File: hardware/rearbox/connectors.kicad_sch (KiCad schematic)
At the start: 6 parts, among them J3 Autosport, J4 Auxiliary

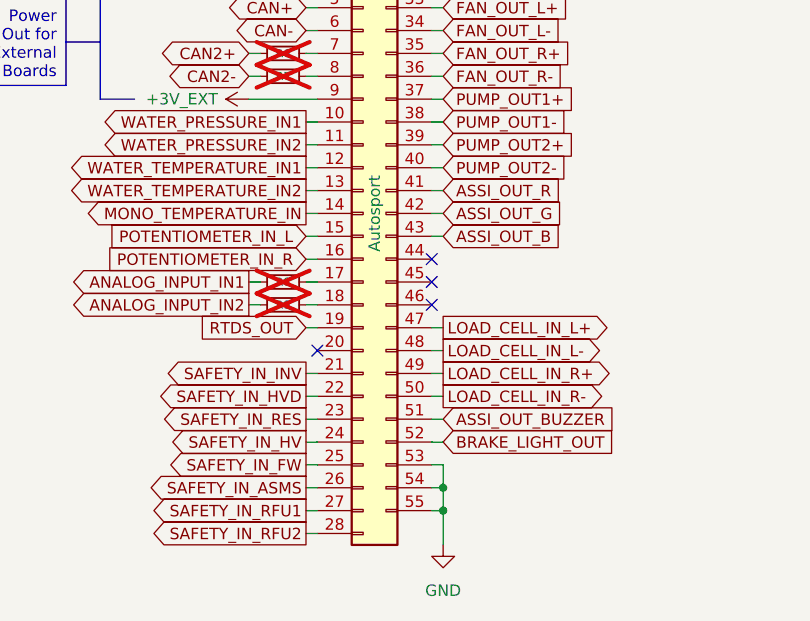
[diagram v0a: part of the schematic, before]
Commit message: Add the connector board
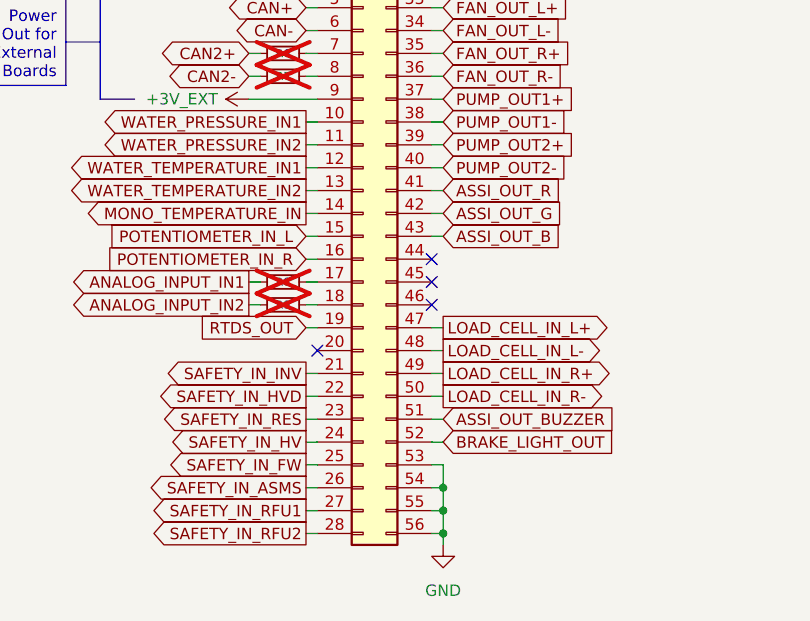
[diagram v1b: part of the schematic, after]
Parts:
- removed J3: Autosport, Local_Library:AS022-55SN, symbol AS022-55SN:AS022-55SN
- added J3: Conn_02x28_Top_Bottom, Connector_PinSocket_2.54mm:PinSocket_2x28_P2.54mm_Horizontal, symbol Connector_Generic:Conn_02x28_Top_Bottom
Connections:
- net +24V: now also J3.1 (Pin_1), J3.2 (Pin_2), J3.3 (Pin_3)
- net +3V_EXT: now also J3.9 (Pin_9)
- net +5V_EXT: now also J3.4 (Pin_4)
- net ASSI_OUT_B: now also J3.43 (Pin_43)
- net ASSI_OUT_BUZZER: now also J3.51 (Pin_51)
- net ASSI_OUT_G: now also J3.42 (Pin_42)
- net ASSI_OUT_R: now also J3.41 (Pin_41)
- net BRAKE_LIGHT_OUT: now also J3.52 (Pin_52)
- net CAN+: now also J3.5 (Pin_5)
- net CAN-: now also J3.6 (Pin_6)
- net FAN_OUT_L+: now also J3.33 (Pin_33)
- net FAN_OUT_L-: now also J3.34 (Pin_34)
- net FAN_OUT_R+: now also J3.35 (Pin_35)
- net FAN_OUT_R-: now also J3.36 (Pin_36)
- net GND: now also J3.53 (Pin_53), J3.54 (Pin_54), J3.55 (Pin_55), J3.56 (Pin_56)
- net LOAD_CELL_IN_L+: now also J3.47 (Pin_47)
- net LOAD_CELL_IN_L-: now also J3.48 (Pin_48)
- net LOAD_CELL_IN_R+: now also J3.49 (Pin_49)
- net LOAD_CELL_IN_R-: now also J3.50 (Pin_50)
- net MONO_TEMPERATURE_IN: now also J3.14 (Pin_14)
- net POTENTIOMETER_IN_L: now also J3.15 (Pin_15)
- net POTENTIOMETER_IN_R: now also J3.16 (Pin_16)
- net PUMP_OUT1+: now also J3.37 (Pin_37)
- net PUMP_OUT1-: now also J3.38 (Pin_38)
- net PUMP_OUT2+: now also J3.39 (Pin_39)
- net PUMP_OUT2-: now also J3.40 (Pin_40)
- net RTDS_OUT: now also J3.19 (Pin_19)
- net SAFETY_IN_ASMS: now also J3.26 (Pin_26)
- net SAFETY_IN_FW: now also J3.25 (Pin_25)
- net SAFETY_IN_HV: now also J3.24 (Pin_24)
- net SAFETY_IN_HVD: now also J3.22 (Pin_22)
- net SAFETY_IN_INV: now also J3.21 (Pin_21)
- net SAFETY_IN_RES: now also J3.23 (Pin_23)
- net SAFETY_IN_RFU1: now also J3.27 (Pin_27)
- net SAFETY_IN_RFU2: now also J3.28 (Pin_28)
- net SAFETY_IN_WHEEL_FL: now also J3.29 (Pin_29)
- net SAFETY_IN_WHEEL_FR: now also J3.30 (Pin_30)
- net SAFETY_IN_WHEEL_RL: now also J3.31 (Pin_31)
- net SAFETY_IN_WHEEL_RR: now also J3.32 (Pin_32)
- net WATER_PRESSURE_IN1: now also J3.10 (Pin_10)
- net WATER_PRESSURE_IN2: now also J3.11 (Pin_11)
- net WATER_TEMPERATURE_IN1: now also J3.12 (Pin_12)
- net WATER_TEMPERATURE_IN2: now also J3.13 (Pin_13)
- net at R6.2: now also J3.7 (Pin_7)
- net at R8.2: now also J3.17 (Pin_17)
- net at R9.2: now also J3.18 (Pin_18)
- net at R7.2: now also J3.8 (Pin_8)
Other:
- title: Autosport -> Connectors

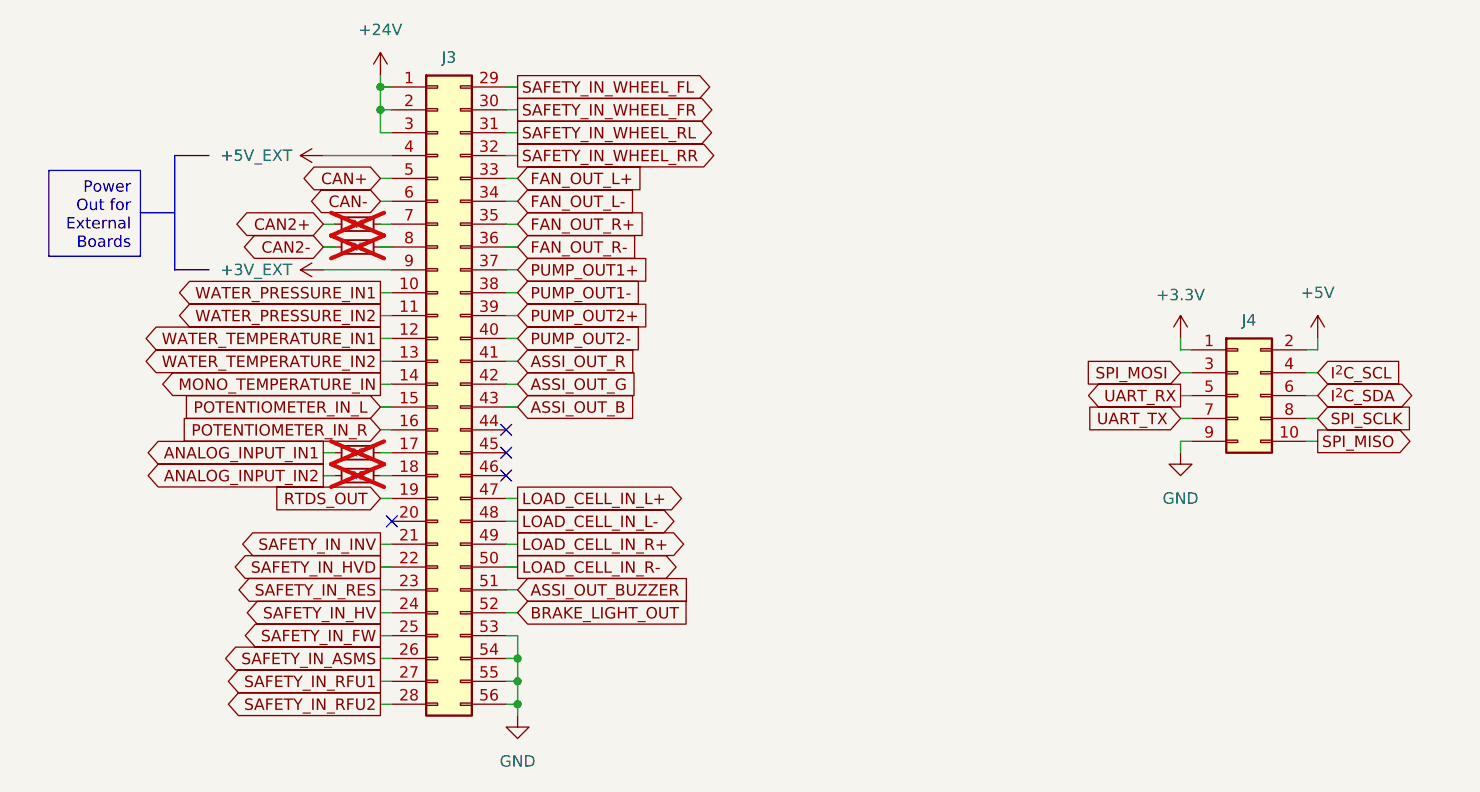
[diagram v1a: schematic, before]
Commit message: Place components on the PCB
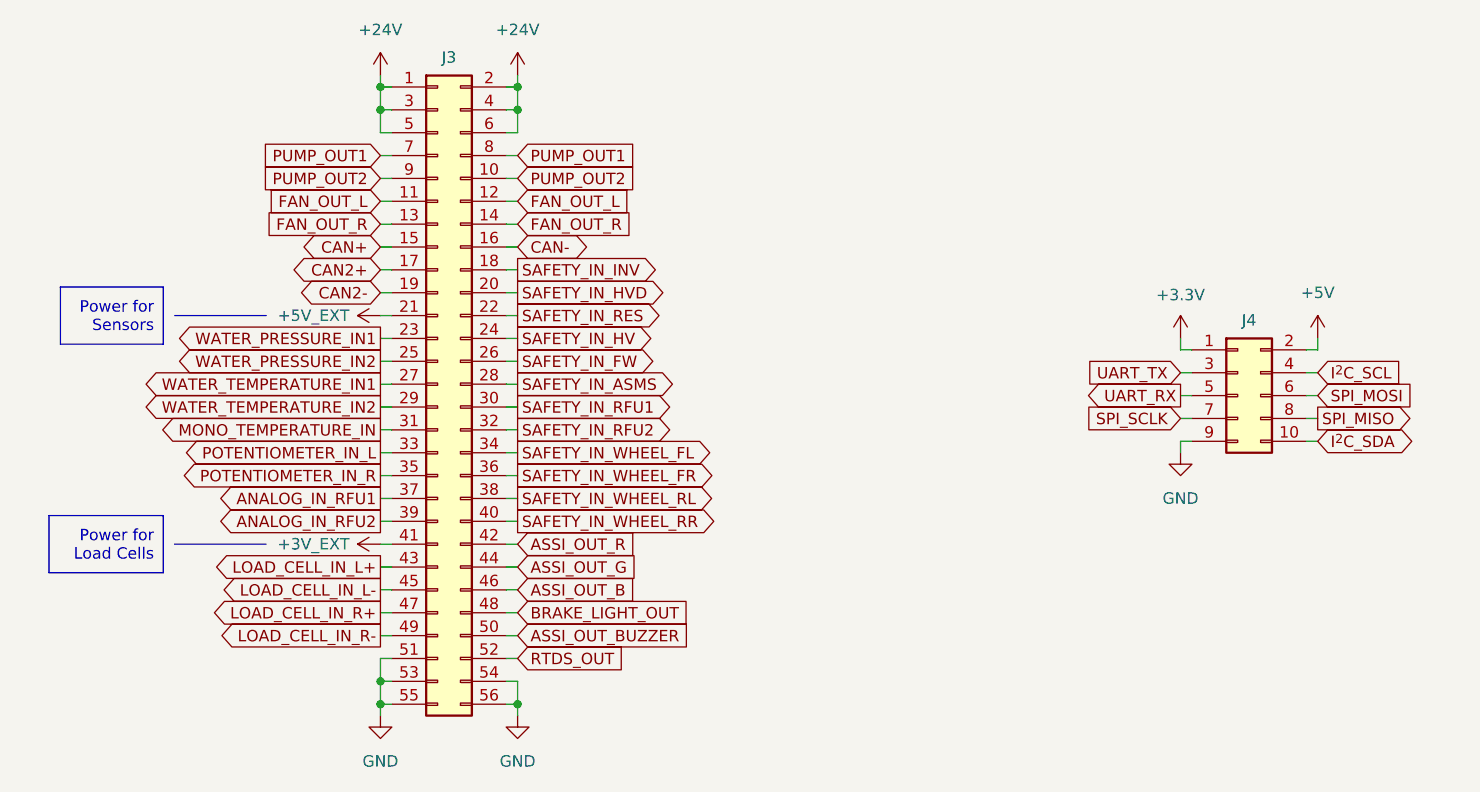
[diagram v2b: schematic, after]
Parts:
- removed R6, R7, R8, R9: 0R, Resistor_SMD:R_0603_1608Metric, symbol Device:R_Small
- J3: footprint Connector_PinSocket_2.54mm:PinSocket_2x28_P2.54mm_Horizontal -> Connector_PinHeader_2.00mm:PinHeader_2x28_P2.00mm_Horizontal; symbol Connector_Generic:Conn_02x28_Top_Bottom -> Connector_Generic:Conn_02x28_Odd_Even
- J4: footprint Connector_PinHeader_2.54mm:PinHeader_2x05_P2.54mm_Vertical_SMD -> Connector_PinHeader_1.27mm:PinHeader_2x05_P1.27mm_Vertical
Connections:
- net FAN_OUT_L+ is gone; now on net POTENTIOMETER_IN_L: J3.33 (Pin_33)
- net FAN_OUT_L- is gone; now on net SAFETY_IN_WHEEL_FL: J3.34 (Pin_34)
- net FAN_OUT_R+ is gone; now on net POTENTIOMETER_IN_R: J3.35 (Pin_35)
- net FAN_OUT_R- is gone; now on net SAFETY_IN_WHEEL_FR: J3.36 (Pin_36)
- net PUMP_OUT1- is gone; now on net SAFETY_IN_WHEEL_RL: J3.38 (Pin_38)
- net PUMP_OUT2- is gone; now on net SAFETY_IN_WHEEL_RR: J3.40 (Pin_40)
- net +24V: now also J3.4 (Pin_4), J3.5 (Pin_5), J3.6 (Pin_6)
- net +3V_EXT: now also J3.41 (Pin_41); no longer J3.9 (Pin_9)
- net +5V_EXT: now also J3.21 (Pin_21); no longer J3.4 (Pin_4)
- net ASSI_OUT_B: now also J3.46 (Pin_46); no longer J3.43 (Pin_43)
- net ASSI_OUT_BUZZER: now also J3.50 (Pin_50); no longer J3.51 (Pin_51)
- net ASSI_OUT_G: now also J3.44 (Pin_44); no longer J3.42 (Pin_42)
- net ASSI_OUT_R: now also J3.42 (Pin_42); no longer J3.41 (Pin_41)
- net BRAKE_LIGHT_OUT: now also J3.48 (Pin_48); no longer J3.52 (Pin_52)
- net CAN+: now also J3.15 (Pin_15); no longer J3.5 (Pin_5)
- net CAN-: now also J3.16 (Pin_16); no longer J3.6 (Pin_6)
- net CAN2+: now also J3.17 (Pin_17)
- net CAN2-: now also J3.19 (Pin_19)
- net GND: now also J3.51 (Pin_51)
- net I^{2}C_SDA: now also J4.10 (Pin_10); no longer J4.6 (Pin_6)
- net LOAD_CELL_IN_L+: now also J3.43 (Pin_43); no longer J3.47 (Pin_47)
- net LOAD_CELL_IN_L-: now also J3.45 (Pin_45); no longer J3.48 (Pin_48)
- net LOAD_CELL_IN_R+: now also J3.47 (Pin_47); no longer J3.49 (Pin_49)
- net LOAD_CELL_IN_R-: now also J3.49 (Pin_49); no longer J3.50 (Pin_50)
- net MONO_TEMPERATURE_IN: now also J3.31 (Pin_31); no longer J3.14 (Pin_14)
- net POTENTIOMETER_IN_L: no longer J3.15 (Pin_15)
- net POTENTIOMETER_IN_R: no longer J3.16 (Pin_16)
- net RTDS_OUT: now also J3.52 (Pin_52); no longer J3.19 (Pin_19)
- net SAFETY_IN_ASMS: now also J3.28 (Pin_28); no longer J3.26 (Pin_26)
- net SAFETY_IN_FW: now also J3.26 (Pin_26); no longer J3.25 (Pin_25)
- net SAFETY_IN_HVD: now also J3.20 (Pin_20); no longer J3.22 (Pin_22)
- net SAFETY_IN_INV: now also J3.18 (Pin_18); no longer J3.21 (Pin_21)
- net SAFETY_IN_RES: now also J3.22 (Pin_22); no longer J3.23 (Pin_23)
- net SAFETY_IN_RFU1: now also J3.30 (Pin_30); no longer J3.27 (Pin_27)
- net SAFETY_IN_RFU2: now also J3.32 (Pin_32); no longer J3.28 (Pin_28)
- net SAFETY_IN_WHEEL_FL: no longer J3.29 (Pin_29)
- net SAFETY_IN_WHEEL_FR: no longer J3.30 (Pin_30)
- net SAFETY_IN_WHEEL_RL: no longer J3.31 (Pin_31)
- net SAFETY_IN_WHEEL_RR: no longer J3.32 (Pin_32)
- net SPI_MISO: now also J4.8 (Pin_8); no longer J4.10 (Pin_10)
- net SPI_MOSI: now also J4.6 (Pin_6); no longer J4.3 (Pin_3)
- net SPI_SCLK: now also J4.7 (Pin_7); no longer J4.8 (Pin_8)
- net UART_TX: now also J4.3 (Pin_3); no longer J4.7 (Pin_7)
- net WATER_PRESSURE_IN1: now also J3.23 (Pin_23); no longer J3.10 (Pin_10)
- net WATER_PRESSURE_IN2: now also J3.25 (Pin_25); no longer J3.11 (Pin_11)
- net WATER_TEMPERATURE_IN1: now also J3.27 (Pin_27); no longer J3.12 (Pin_12)
- net WATER_TEMPERATURE_IN2: now also J3.29 (Pin_29); no longer J3.13 (Pin_13)
- net PUMP_OUT1: now reaches J3.7 (Pin_7)
- net PUMP_OUT1: now also J3.8 (Pin_8)
- net PUMP_OUT1+ renamed ANALOG_IN_RFU1
- net PUMP_OUT2+ renamed ANALOG_IN_RFU2
- new net FAN_OUT_L: J3.11 (Pin_11), J3.12 (Pin_12)
- new net FAN_OUT_R: J3.13 (Pin_13), J3.14 (Pin_14)
- new net PUMP_OUT2: J3.10 (Pin_10), J3.9 (Pin_9)
- no-connect marks 4 -> 0

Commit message: Align footprint references
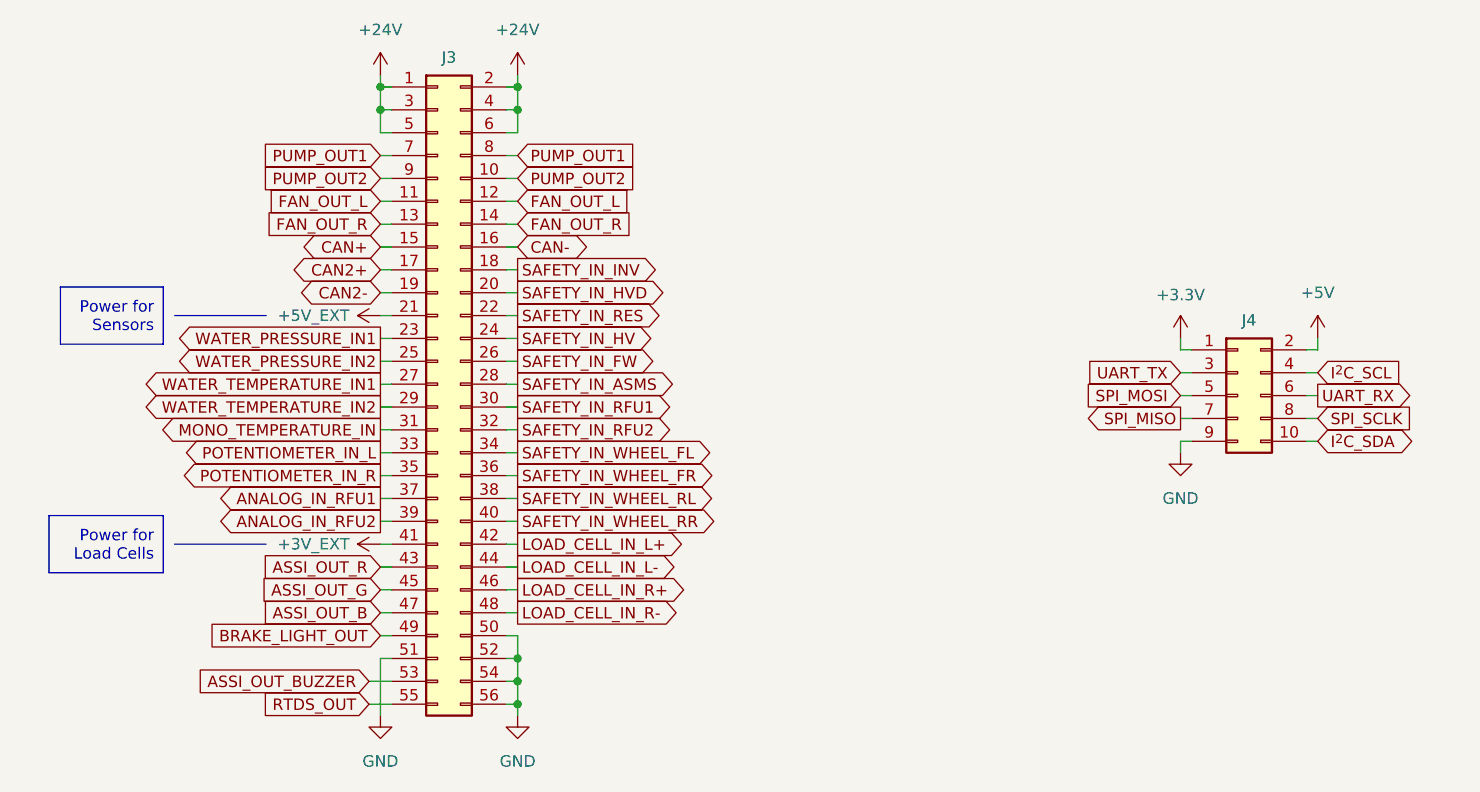
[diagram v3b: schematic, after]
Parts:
- J4: footprint Connector_PinHeader_1.27mm:PinHeader_2x05_P1.27mm_Vertical -> Connector_PinHeader_1.27mm:PinHeader_2x05_P1.27mm_Vertical_SMD
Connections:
- net ASSI_OUT_B: now also J3.47 (Pin_47); no longer J3.46 (Pin_46)
- net ASSI_OUT_BUZZER: now also J3.53 (Pin_53); no longer J3.50 (Pin_50)
- net ASSI_OUT_G: now also J3.45 (Pin_45); no longer J3.44 (Pin_44)
- net ASSI_OUT_R: now also J3.43 (Pin_43); no longer J3.42 (Pin_42)
- net BRAKE_LIGHT_OUT: now also J3.49 (Pin_49); no longer J3.48 (Pin_48)
- net GND: now also J3.50 (Pin_50), J3.52 (Pin_52); no longer J3.53 (Pin_53), J3.55 (Pin_55)
- net LOAD_CELL_IN_L+: now also J3.42 (Pin_42); no longer J3.43 (Pin_43)
- net LOAD_CELL_IN_L-: now also J3.44 (Pin_44); no longer J3.45 (Pin_45)
- net LOAD_CELL_IN_R+: now also J3.46 (Pin_46); no longer J3.47 (Pin_47)
- net LOAD_CELL_IN_R-: now also J3.48 (Pin_48); no longer J3.49 (Pin_49)
- net RTDS_OUT: now also J3.55 (Pin_55); no longer J3.52 (Pin_52)
- net SPI_MISO: now also J4.7 (Pin_7); no longer J4.8 (Pin_8)
- net SPI_MOSI: now also J4.5 (Pin_5); no longer J4.6 (Pin_6)
- net SPI_SCLK: now also J4.8 (Pin_8); no longer J4.7 (Pin_7)
- net UART_RX: now also J4.6 (Pin_6); no longer J4.5 (Pin_5)
